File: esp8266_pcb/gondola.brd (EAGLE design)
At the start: 75 x 42 mm, 22 parts, among them X1 1751248, X2 1751264

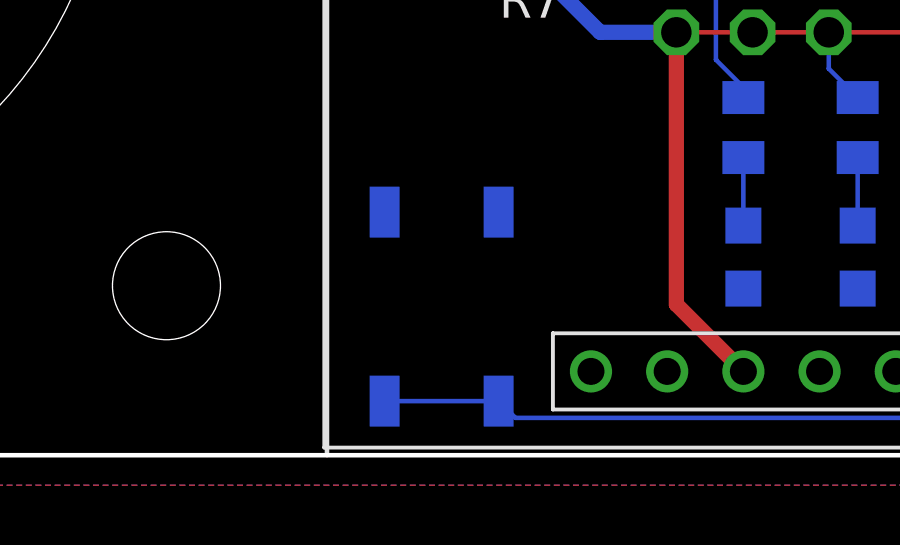
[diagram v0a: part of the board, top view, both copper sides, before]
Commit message: deleted old layout. Corrected footbrint of button. Changed pins to Adafruit HUZZAH. Added RSSI measurements
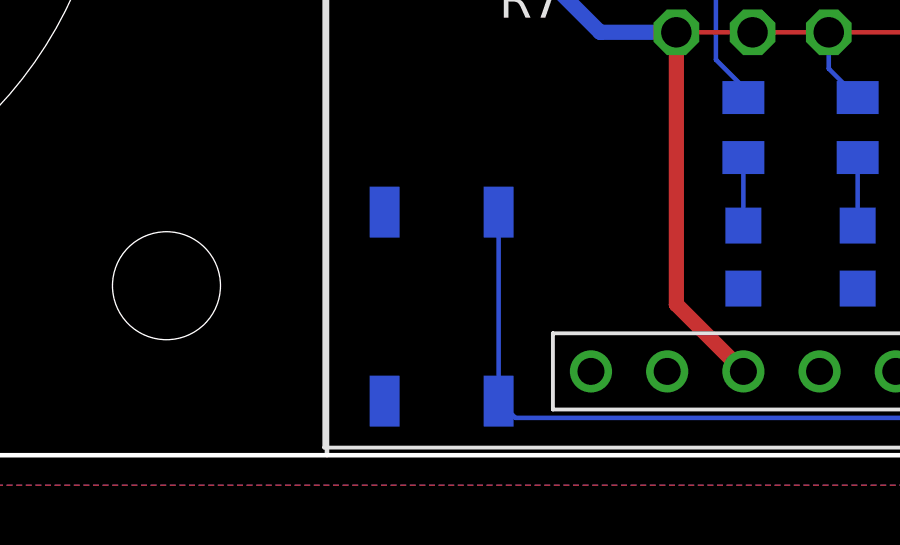
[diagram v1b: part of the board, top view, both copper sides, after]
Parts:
- renumbered U$3 to U1
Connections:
- net GND: now also U$4.2; no longer U$4.3
- net SW_BUT: now also U$4.3; no longer U$4.2
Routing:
- net SW_BUT: track 23.5 -> 26.0 mm
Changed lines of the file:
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@@
 <setting verticaltext="up"/>
 </settings>
-<grid distance="1" unitdist="mil" unit="mil" style="lines" multiple="1" display="yes" altdistance="3.93700787" altunitdist="mil" altunit="mil"/>
+<grid distance="1" unitdist="mil" unit="mm" style="lines" multiple="1" display="yes" altdistance="0.0999999999" altunitdist="mm" altunit="mm"/>
 <layers>
 <layer number="1" name="Top" color="4" fill="1" visible="yes" active="yes"/>
@@
 <attribute name="OC_NEWARK" value="10R0934" x="49.883059375" y="38.1508" size="1.778" layer="27" display="off"/>
 </element>
-<element name="U$3" library="MS" package="ROHM_BP5293-XX" value="ROHM_BP5293-XX" x="52.696" y="27.388" rot="R180"/>
+<element name="U1" library="MS" package="ROHM_BP5293-XX" value="ROHM_BP5293-XX" x="52.696" y="27.388" rot="R180"/>
 <element name="LED3_5V" library="led" library_urn="urn:adsk.eagle:library:259" package="CHIP-LED0805" package3d_urn="urn:adsk.eagle:package:15818/1" value="" x="55.88" y="6.604" smashed="yes" rot="MR180">
 <attribute name="VALUE" x="58.42" y="7.874" size="1.27" layer="28" rot="MR270"/>
@@
 <contactref element="U$1" pad="GND@0"/>
 <contactref element="U$2" pad="1_GND"/>
-<contactref element="U$3" pad="GND"/>
+<contactref element="U1" pad="GND"/>
 <contactref element="U$2" pad="10_GND"/>
 <contactref element="D1" pad="A"/>
@@
 <vertex x="79" y="44"/>
 </polygon>
+<contactref element="U$4" pad="2"/>
 <contactref element="U$4" pad="1"/>
-<contactref element="U$4" pad="3"/>
 </signal>
 <signal name="MS1">
@@
 <contactref element="U$1" pad="VMOT"/>
 <contactref element="C1" pad="+"/>
-<contactref element="U$3" pad="VIN"/>
+<contactref element="U1" pad="VIN"/>
 <contactref element="D1" pad="C"/>
 <contactref element="R2" pad="2"/>
@@
 </signal>
 <signal name="+5V">
-<contactref element="U$3" pad="VOUT"/>
+<contactref element="U1" pad="VOUT"/>
 <contactref element="U$2" pad="9_VBAT"/>
 <contactref element="R3" pad="2"/>
@@
 <contactref element="U$2" pad="7_GPIO4"/>
 <contactref element="U$4" pad="4"/>
-<contactref element="U$4" pad="2"/>
-<wire x1="47.7216" y1="1.803" x2="43.9216" y2="1.803" width="0.1524" layer="16"/>
 <wire x1="66.04" y1="2.794" x2="66.04" y2="1.8796" width="0.1524" layer="16"/>
 <wire x1="66.04" y1="1.8796" x2="65.405" y2="1.2446" width="0.1524" layer="16"/>
 <wire x1="65.405" y1="1.2446" x2="48.28" y2="1.2446" width="0.1524" layer="16"/>
-<wire x1="48.28" y1="1.2446" x2="47.7216" y2="1.803" width="0.1524" layer="16"/>
+<wire x1="47.7216" y1="1.803" x2="48.28" y2="1.2446" width="0.1524" layer="16"/>
+<contactref element="U$4" pad="3"/>
+<wire x1="47.7216" y1="8.103" x2="47.7216" y2="1.803" width="0.1524" layer="16"/>
 </signal>
 <signal name="N$1">
